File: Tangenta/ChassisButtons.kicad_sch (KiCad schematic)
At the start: 26 parts, among them J2 Conn_02x02_Top_Bottom, Q1 2N7002, Q2 2N7002, SW1 TSC015A04818B, SW2 TSC015A04818B, U7 74HC04D,653, U8 CD4060SA_TR, U9 74HC74D,653

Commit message: Removing component association with previous project (local) libraries.
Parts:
- C34, C35, C36, C37, C38, C39: symbol CholaSymbolsPrjLib:C_Small -> C_Small:C_Small
- J2: symbol CholaSymbolsPrjLib:Conn_02x02_Top_Bottom -> Conn_02x02_Top_Bottom:Conn_02x02_Top_Bottom
- Q1, Q2: footprint CholaFootprintsPrjLib:NMOS_2N7002 -> NMOS_2N7002:NMOS_2N7002; symbol CholaSymbolsPrjLib:2N7002 -> 2N7002:2N7002
- R15, R16, R17, R18, R19, R20, R21, R22, R23, R24, R25, R26: symbol CholaSymbolsPrjLib:R_Small_US -> R_Small_US:R_Small_US
- SW1, SW2: footprint CholaFootprintsPrjLib:Tactile_BTN -> Tactile_BTN:Tactile_BTN; symbol CholaSymbolsPrjLib:TSC015A04818B -> TSC015A04818B:TSC015A04818B
- U7: footprint CholaFootprintsPrjLib:74HC04D -> 74HC04D:74HC04D; symbol CholaSymbolsPrjLib:74HC04D,653 -> 74HC04D,653:74HC04D,653
- U8: footprint CholaFootprintsPrjLib:CD4060 -> CD4060:CD4060; symbol CholaSymbolsPrjLib:CD4060SA_TR -> CD4060SA_TR:CD4060SA_TR
- U9: footprint CholaFootprintsPrjLib:74HC74D -> 74HC74D:74HC74D; symbol CholaSymbolsPrjLib:74HC74D,653 -> 74HC74D,653:74HC74D,653
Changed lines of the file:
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@@
 	)
 	(symbol
-		(lib_id "CholaSymbolsPrjLib:R_Small_US")
+		(lib_id "R_Small_US:R_Small_US")
 		(at 68.58 74.93 0)
 		(unit 1)
@@
 	)
 	(symbol
-		(lib_id "CholaSymbolsPrjLib:74HC04D,653")
+		(lib_id "74HC04D,653:74HC04D,653")
 		(at 141.605 66.04 0)
 		(unit 1)
@@
 			)
 		)
-		(property "Footprint" "CholaFootprintsPrjLib:74HC04D"
+		(property "Footprint" "74HC04D:74HC04D"
 			(at 142.748 82.931 0)
 			(effects
@@
 	)
 	(symbol
-		(lib_id "CholaSymbolsPrjLib:R_Small_US")
+		(lib_id "R_Small_US:R_Small_US")
 		(at 215.265 121.285 90)
 		(unit 1)
@@
 	)
 	(symbol
-		(lib_id "CholaSymbolsPrjLib:C_Small")
+		(lib_id "C_Small:C_Small")
 		(at 142.24 82.55 90)
 		(unit 1)
@@
 	)
 	(symbol
-		(lib_id "CholaSymbolsPrjLib:R_Small_US")
+		(lib_id "R_Small_US:R_Small_US")
 		(at 168.275 116.205 90)
 		(unit 1)
@@
 	)
 	(symbol
-		(lib_id "CholaSymbolsPrjLib:TSC015A04818B")
+		(lib_id "TSC015A04818B:TSC015A04818B")
 		(at 60.833 111.125 90)
 		(unit 1)
@@
 			)
 		)
-		(property "Footprint" "CholaFootprintsPrjLib:Tactile_BTN"
+		(property "Footprint" "Tactile_BTN:Tactile_BTN"
 			(at 71.501 114.554 0)
 			(effects
@@
 	)
 	(symbol
-		(lib_id "CholaSymbolsPrjLib:C_Small")
+		(lib_id "C_Small:C_Small")
 		(at 215.265 82.55 90)
 		(unit 1)
@@
 	)
 	(symbol
-		(lib_id "CholaSymbolsPrjLib:74HC74D,653")
+		(lib_id "74HC74D,653:74HC74D,653")
 		(at 215.011 66.167 0)
 		(unit 1)
@@
 			)
 		)
-		(property "Footprint" "CholaFootprintsPrjLib:74HC74D"
+		(property "Footprint" "74HC74D:74HC74D"
 			(at 216.408 82.931 0)
 			(effects
@@
 	)
 	(symbol
-		(lib_id "CholaSymbolsPrjLib:R_Small_US")
+		(lib_id "R_Small_US:R_Small_US")
 		(at 103.505 83.82 90)
 		(unit 1)
@@
 	)
 	(symbol
-		(lib_id "CholaSymbolsPrjLib:Conn_02x02_Top_Bottom")
+		(lib_id "Conn_02x02_Top_Bottom:Conn_02x02_Top_Bottom")
 		(at 76.2 83.82 0)
 		(unit 1)
@@
 	)
 	(symbol
-		(lib_id "CholaSymbolsPrjLib:CD4060SA_TR")
+		(lib_id "CD4060SA_TR:CD4060SA_TR")
 		(at 141.605 109.855 0)
 		(unit 1)
@@
 			)
 		)
-		(property "Footprint" "CholaFootprintsPrjLib:CD4060"
+		(property "Footprint" "CD4060:CD4060"
 			(at 141.605 128.524 0)
 			(effects
@@
 	)
 	(symbol
-		(lib_id "CholaSymbolsPrjLib:R_Small_US")
+		(lib_id "R_Small_US:R_Small_US")
 		(at 237.49 109.855 0)
 		(unit 1)
@@
 	)
 	(symbol
-		(lib_id "CholaSymbolsPrjLib:R_Small_US")
+		(lib_id "R_Small_US:R_Small_US")
 		(at 86.36 74.93 0)
 		(unit 1)
@@
 	)
 	(symbol
-		(lib_id "CholaSymbolsPrjLib:C_Small")
+		(lib_id "C_Small:C_Small")
 		(at 69.215 111.125 0)
 		(mirror x)
@@
 	)
 	(symbol
-		(lib_id "CholaSymbolsPrjLib:2N7002")
+		(lib_id "2N7002:2N7002")
 		(at 224.155 121.285 0)
 		(unit 1)
@@
 			)
 		)
-		(property "Footprint" "CholaFootprintsPrjLib:NMOS_2N7002"
+		(property "Footprint" "NMOS_2N7002:NMOS_2N7002"
 			(at 215.392 139.954 0)
 			(effects
@@
 	)
 	(symbol
-		(lib_id "CholaSymbolsPrjLib:R_Small_US")
+		(lib_id "R_Small_US:R_Small_US")
 		(at 211.455 128.905 0)
 		(unit 1)
@@
 	)
 	(symbol
-		(lib_id "CholaSymbolsPrjLib:R_Small_US")
+		(lib_id "R_Small_US:R_Small_US")
 		(at 252.73 81.28 0)
 		(unit 1)
@@
 	)
 	(symbol
-		(lib_id "CholaSymbolsPrjLib:R_Small_US")
+		(lib_id "R_Small_US:R_Small_US")
 		(at 191.135 60.96 270)
 		(unit 1)
@@
 	)
 	(symbol
-		(lib_id "CholaSymbolsPrjLib:R_Small_US")
+		(lib_id "R_Small_US:R_Small_US")
 		(at 168.275 111.76 90)
 		(unit 1)
@@
 	)
 	(symbol
-		(lib_id "CholaSymbolsPrjLib:R_Small_US")
+		(lib_id "R_Small_US:R_Small_US")
 		(at 52.07 83.82 90)
 		(unit 1)
@@
 	)
 	(symbol
-		(lib_id "CholaSymbolsPrjLib:R_Small_US")
+		(lib_id "R_Small_US:R_Small_US")
 		(at 241.3 102.235 90)
 		(unit 1)
@@
 	)
 	(symbol
-		(lib_id "CholaSymbolsPrjLib:TSC015A04818B")
+		(lib_id "TSC015A04818B:TSC015A04818B")
 		(at 87.122 111.125 270)
 		(mirror x)
@@
 			)
 		)
-		(property "Footprint" "CholaFootprintsPrjLib:Tactile_BTN"
+		(property "Footprint" "Tactile_BTN:Tactile_BTN"
 			(at 76.454 114.554 0)
 			(effects
@@
 	)
 	(symbol
-		(lib_id "CholaSymbolsPrjLib:C_Small")
+		(lib_id "C_Small:C_Small")
 		(at 168.275 120.65 90)
 		(unit 1)
@@
 	)
 	(symbol
-		(lib_id "CholaSymbolsPrjLib:C_Small")
+		(lib_id "C_Small:C_Small")
 		(at 78.74 111.125 0)
 		(mirror x)
@@
 	)
 	(symbol
-		(lib_id "CholaSymbolsPrjLib:2N7002")
+		(lib_id "2N7002:2N7002")
 		(at 250.19 102.235 0)
 		(unit 1)
@@
 			)
 		)
-		(property "Footprint" "CholaFootprintsPrjLib:NMOS_2N7002"
+		(property "Footprint" "NMOS_2N7002:NMOS_2N7002"
 			(at 241.427 120.904 0)
 			(effects
@@
 	)
 	(symbol
-		(lib_id "CholaSymbolsPrjLib:C_Small")
+		(lib_id "C_Small:C_Small")
 		(at 142.24 127.635 90)
 		(unit 1)

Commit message: Fixes, before checks.
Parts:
- C34, C35, C36, C37, C38, C39: symbol C_Small:C_Small -> Device:C_Small
- J2: symbol Conn_02x02_Top_Bottom:Conn_02x02_Top_Bottom -> Connector_Generic:Conn_02x02_Top_Bottom
- Q1, Q2: symbol 2N7002:2N7002 -> NMOS_2N7002:2N7002
- R15, R16, R17, R18, R19, R20, R21, R22, R23, R24, R25, R26: symbol R_Small_US:R_Small_US -> Device:R_Small_US
- SW1, SW2: symbol TSC015A04818B:TSC015A04818B -> Tactile_BTN:TSC015A04818B
- U7: symbol 74HC04D,653:74HC04D,653 -> 74HC04D:74HC04D,653
- U8: symbol CD4060SA_TR:CD4060SA_TR -> CD4060:CD4060SA_TR
- U9: symbol 74HC74D,653:74HC74D,653 -> 74HC74D:74HC74D,653
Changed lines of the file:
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@@
 	)
 	(symbol
-		(lib_id "R_Small_US:R_Small_US")
+		(lib_id "Device:R_Small_US")
 		(at 68.58 74.93 0)
 		(unit 1)
@@
 	)
 	(symbol
-		(lib_id "74HC04D,653:74HC04D,653")
+		(lib_id "74HC04D:74HC04D,653")
 		(at 141.605 66.04 0)
 		(unit 1)
@@
 	)
 	(symbol
-		(lib_id "R_Small_US:R_Small_US")
+		(lib_id "Device:R_Small_US")
 		(at 215.265 121.285 90)
 		(unit 1)
@@
 	)
 	(symbol
-		(lib_id "C_Small:C_Small")
+		(lib_id "Device:C_Small")
 		(at 142.24 82.55 90)
 		(unit 1)
@@
 	)
 	(symbol
-		(lib_id "R_Small_US:R_Small_US")
+		(lib_id "Device:R_Small_US")
 		(at 168.275 116.205 90)
 		(unit 1)
@@
 	)
 	(symbol
-		(lib_id "TSC015A04818B:TSC015A04818B")
+		(lib_id "Tactile_BTN:TSC015A04818B")
 		(at 60.833 111.125 90)
 		(unit 1)
@@
 	)
 	(symbol
-		(lib_id "C_Small:C_Small")
+		(lib_id "Device:C_Small")
 		(at 215.265 82.55 90)
 		(unit 1)
@@
 	)
 	(symbol
-		(lib_id "74HC74D,653:74HC74D,653")
+		(lib_id "74HC74D:74HC74D,653")
 		(at 215.011 66.167 0)
 		(unit 1)
@@
 	)
 	(symbol
-		(lib_id "R_Small_US:R_Small_US")
+		(lib_id "Device:R_Small_US")
 		(at 103.505 83.82 90)
 		(unit 1)
@@
 	)
 	(symbol
-		(lib_id "Conn_02x02_Top_Bottom:Conn_02x02_Top_Bottom")
+		(lib_id "Connector_Generic:Conn_02x02_Top_Bottom")
 		(at 76.2 83.82 0)
 		(unit 1)
@@
 	)
 	(symbol
-		(lib_id "CD4060SA_TR:CD4060SA_TR")
+		(lib_id "CD4060:CD4060SA_TR")
 		(at 141.605 109.855 0)
 		(unit 1)
@@
 	)
 	(symbol
-		(lib_id "R_Small_US:R_Small_US")
+		(lib_id "Device:R_Small_US")
 		(at 237.49 109.855 0)
 		(unit 1)
@@
 	)
 	(symbol
-		(lib_id "R_Small_US:R_Small_US")
+		(lib_id "Device:R_Small_US")
 		(at 86.36 74.93 0)
 		(unit 1)
@@
 	)
 	(symbol
-		(lib_id "C_Small:C_Small")
+		(lib_id "Device:C_Small")
 		(at 69.215 111.125 0)
 		(mirror x)
@@
 	)
 	(symbol
-		(lib_id "2N7002:2N7002")
+		(lib_id "NMOS_2N7002:2N7002")
 		(at 224.155 121.285 0)
 		(unit 1)
@@
 	)
 	(symbol
-		(lib_id "R_Small_US:R_Small_US")
+		(lib_id "Device:R_Small_US")
 		(at 211.455 128.905 0)
 		(unit 1)
@@
 	)
 	(symbol
-		(lib_id "R_Small_US:R_Small_US")
+		(lib_id "Device:R_Small_US")
 		(at 252.73 81.28 0)
 		(unit 1)
@@
 	)
 	(symbol
-		(lib_id "R_Small_US:R_Small_US")
+		(lib_id "Device:R_Small_US")
 		(at 191.135 60.96 270)
 		(unit 1)
@@
 	)
 	(symbol
-		(lib_id "R_Small_US:R_Small_US")
+		(lib_id "Device:R_Small_US")
 		(at 168.275 111.76 90)
 		(unit 1)
@@
 	)
 	(symbol
-		(lib_id "R_Small_US:R_Small_US")
+		(lib_id "Device:R_Small_US")
 		(at 52.07 83.82 90)
 		(unit 1)
@@
 	)
 	(symbol
-		(lib_id "R_Small_US:R_Small_US")
+		(lib_id "Device:R_Small_US")
 		(at 241.3 102.235 90)
 		(unit 1)
@@
 	)
 	(symbol
-		(lib_id "TSC015A04818B:TSC015A04818B")
+		(lib_id "Tactile_BTN:TSC015A04818B")
 		(at 87.122 111.125 270)
 		(mirror x)
@@
 	)
 	(symbol
-		(lib_id "C_Small:C_Small")
+		(lib_id "Device:C_Small")
 		(at 168.275 120.65 90)
 		(unit 1)
@@
 	)
 	(symbol
-		(lib_id "C_Small:C_Small")
+		(lib_id "Device:C_Small")
 		(at 78.74 111.125 0)
 		(mirror x)
@@
 	)
 	(symbol
-		(lib_id "2N7002:2N7002")
+		(lib_id "NMOS_2N7002:2N7002")
 		(at 250.19 102.235 0)
 		(unit 1)
@@
 	)
 	(symbol
-		(lib_id "C_Small:C_Small")
+		(lib_id "Device:C_Small")
 		(at 142.24 127.635 90)
 		(unit 1)

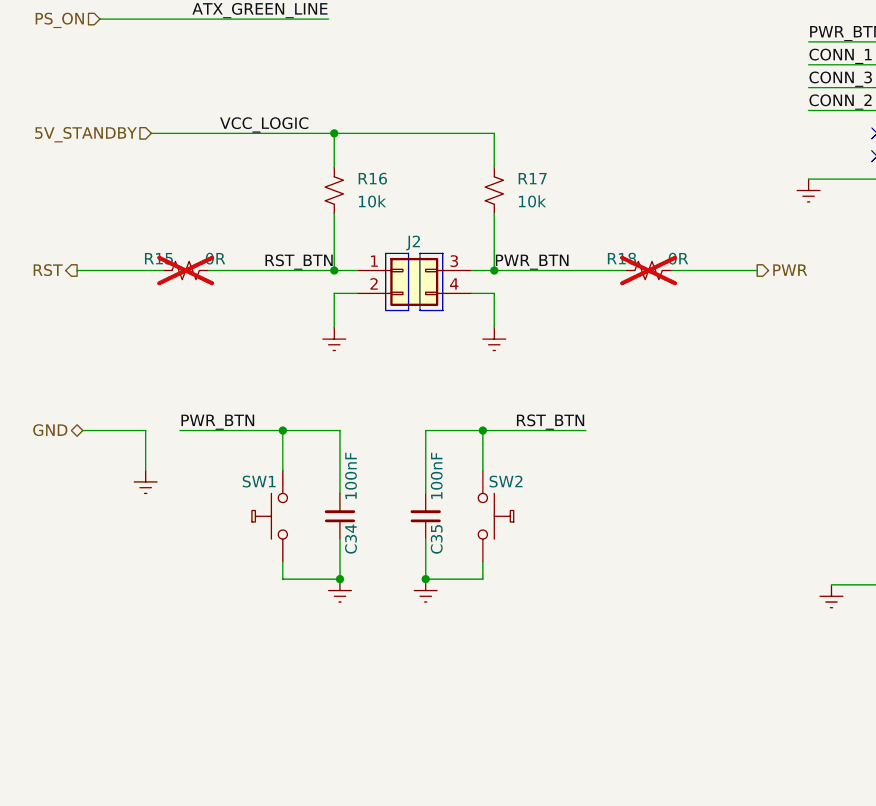
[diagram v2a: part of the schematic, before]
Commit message: Reverting to the original design.
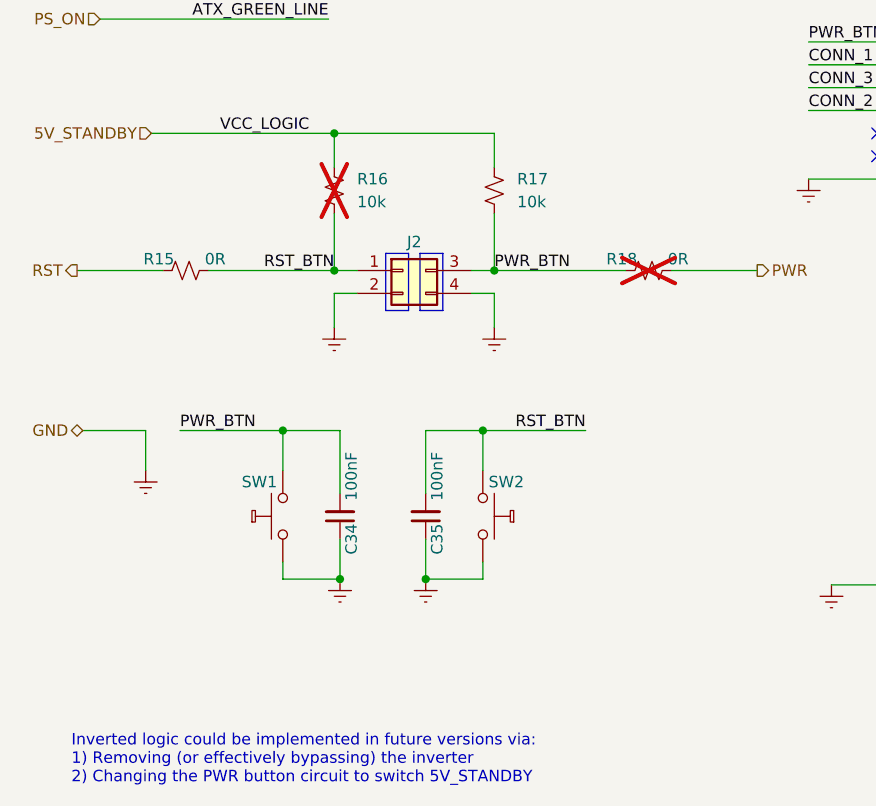
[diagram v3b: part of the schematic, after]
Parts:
- C34, C35, C36, C37, C38, C39: symbol Device:C_Small -> CholaSymbolsPrjLib:C_Small
- J2: symbol Connector_Generic:Conn_02x02_Top_Bottom -> CholaSymbolsPrjLib:Conn_02x02_Top_Bottom
- Q1, Q2: symbol NMOS_2N7002:2N7002 -> CholaSymbolsPrjLib:2N7002
- R15: symbol Device:R_Small_US -> CholaSymbolsPrjLib:R_Small_US; now fitted; now in the parts list
- R16: symbol Device:R_Small_US -> CholaSymbolsPrjLib:R_Small_US; now not fitted; now left out of the parts list
- R17, R18, R19, R20, R21, R22, R23, R24, R25, R26: symbol Device:R_Small_US -> CholaSymbolsPrjLib:R_Small_US
- SW1, SW2: symbol Tactile_BTN:TSC015A04818B -> CholaSymbolsPrjLib:TSC015A04818B
- U7: symbol 74HC04D:74HC04D,653 -> CholaSymbolsPrjLib:74HC04D,653
- U8: symbol CD4060:CD4060SA_TR -> CholaSymbolsPrjLib:CD4060SA_TR
- U9: symbol 74HC74D:74HC74D,653 -> CholaSymbolsPrjLib:74HC74D,653
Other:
- note added: "Inverted logic could be implemented in future versions via: 1) Removing (or effectively bypassing) the inverter 2) Changing the PWR button circuit to switch 5V_STANDBY"

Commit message: ...
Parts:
- C34, C35, C36, C37, C38, C39: symbol CholaSymbolsPrjLib:C_Small -> LocalPrjLib:C_Small
- J2: symbol CholaSymbolsPrjLib:Conn_02x02_Top_Bottom -> LocalPrjLib:Conn_02x02_Top_Bottom
- Q1, Q2: symbol CholaSymbolsPrjLib:2N7002 -> LocalPrjLib:2N7002
- R15, R16, R17, R18, R19, R20, R21, R22, R23, R24, R25, R26: symbol CholaSymbolsPrjLib:R_Small_US -> LocalPrjLib:R_Small_US
- SW1, SW2: symbol CholaSymbolsPrjLib:TSC015A04818B -> LocalPrjLib:TSC015A04818B
- U7: symbol CholaSymbolsPrjLib:74HC04D,653 -> LocalPrjLib:74HC04D,653
- U8: symbol CholaSymbolsPrjLib:CD4060SA_TR -> LocalPrjLib:CD4060SA_TR
- U9: symbol CholaSymbolsPrjLib:74HC74D,653 -> LocalPrjLib:74HC74D,653
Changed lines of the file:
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@@
     )
   )
-  (symbol (lib_id "CholaSymbolsPrjLib:R_Small_US") (at 68.58 74.93 0) (unit 1)
+  (symbol (lib_id "LocalPrjLib:R_Small_US") (at 68.58 74.93 0) (unit 1)
     (in_bom no) (on_board yes) (dnp yes) (fields_autoplaced)
     (property "Reference" "R16" (at 71.12 73.66 0)
@@
     )
   )
-  (symbol (lib_id "CholaSymbolsPrjLib:74HC04D,653") (at 141.605 66.04 0) (unit 1)
+  (symbol (lib_id "LocalPrjLib:74HC04D,653") (at 141.605 66.04 0) (unit 1)
     (in_bom yes) (on_board yes) (dnp no)
     (property "Reference" "U7" (at 135.255 54.61 0)
@@
     )
   )
-  (symbol (lib_id "CholaSymbolsPrjLib:R_Small_US") (at 215.265 121.285 90) (unit 1)
+  (symbol (lib_id "LocalPrjLib:R_Small_US") (at 215.265 121.285 90) (unit 1)
     (in_bom yes) (on_board yes) (dnp no)
     (property "Reference" "R23" (at 212.725 120.015 90)
@@
     )
   )
-  (symbol (lib_id "CholaSymbolsPrjLib:C_Small") (at 142.24 82.55 90) (unit 1)
+  (symbol (lib_id "LocalPrjLib:C_Small") (at 142.24 82.55 90) (unit 1)
     (in_bom yes) (on_board yes) (dnp no)
     (property "Reference" "C36" (at 139.065 83.82 90)
@@
     )
   )
-  (symbol (lib_id "CholaSymbolsPrjLib:R_Small_US") (at 168.275 116.205 90) (unit 1)
+  (symbol (lib_id "LocalPrjLib:R_Small_US") (at 168.275 116.205 90) (unit 1)
     (in_bom yes) (on_board yes) (dnp no)
     (property "Reference" "R20" (at 165.735 114.935 90)
@@
     )
   )
-  (symbol (lib_id "CholaSymbolsPrjLib:TSC015A04818B") (at 60.833 111.125 90) (unit 1)
+  (symbol (lib_id "LocalPrjLib:TSC015A04818B") (at 60.833 111.125 90) (unit 1)
     (in_bom yes) (on_board yes) (dnp no)
     (property "Reference" "SW1" (at 58.293 107.315 90)
@@
     )
   )
-  (symbol (lib_id "CholaSymbolsPrjLib:C_Small") (at 215.265 82.55 90) (unit 1)
+  (symbol (lib_id "LocalPrjLib:C_Small") (at 215.265 82.55 90) (unit 1)
     (in_bom yes) (on_board yes) (dnp no)
     (property "Reference" "C39" (at 212.09 83.82 90)
@@
     )
   )
-  (symbol (lib_id "CholaSymbolsPrjLib:74HC74D,653") (at 215.011 66.167 0) (unit 1)
+  (symbol (lib_id "LocalPrjLib:74HC74D,653") (at 215.011 66.167 0) (unit 1)
     (in_bom yes) (on_board yes) (dnp no)
     (property "Reference" "U9" (at 208.661 54.737 0)
@@
     )
   )
-  (symbol (lib_id "CholaSymbolsPrjLib:R_Small_US") (at 103.505 83.82 90) (unit 1)
+  (symbol (lib_id "LocalPrjLib:R_Small_US") (at 103.505 83.82 90) (unit 1)
     (in_bom no) (on_board yes) (dnp yes)
     (property "Reference" "R18" (at 102.235 82.55 90)
@@
     )
   )
-  (symbol (lib_id "CholaSymbolsPrjLib:Conn_02x02_Top_Bottom") (at 76.2 83.82 0) (unit 1)
+  (symbol (lib_id "LocalPrjLib:Conn_02x02_Top_Bottom") (at 76.2 83.82 0) (unit 1)
     (in_bom yes) (on_board yes) (dnp no)
     (property "Reference" "J2" (at 77.47 80.645 0)
@@
     )
   )
-  (symbol (lib_id "CholaSymbolsPrjLib:CD4060SA_TR") (at 141.605 109.855 0) (unit 1)
+  (symbol (lib_id "LocalPrjLib:CD4060SA_TR") (at 141.605 109.855 0) (unit 1)
     (in_bom yes) (on_board yes) (dnp no)
     (property "Reference" "U8" (at 135.255 97.155 0)
@@
     )
   )
-  (symbol (lib_id "CholaSymbolsPrjLib:R_Small_US") (at 237.49 109.855 0) (unit 1)
+  (symbol (lib_id "LocalPrjLib:R_Small_US") (at 237.49 109.855 0) (unit 1)
     (in_bom yes) (on_board yes) (dnp no)
     (property "Reference" "R24" (at 238.76 108.585 0)
@@
     )
   )
-  (symbol (lib_id "CholaSymbolsPrjLib:R_Small_US") (at 86.36 74.93 0) (unit 1)
+  (symbol (lib_id "LocalPrjLib:R_Small_US") (at 86.36 74.93 0) (unit 1)
     (in_bom yes) (on_board yes) (dnp no) (fields_autoplaced)
     (property "Reference" "R17" (at 88.9 73.66 0)
@@
     )
   )
-  (symbol (lib_id "CholaSymbolsPrjLib:C_Small") (at 69.215 111.125 0) (mirror x) (unit 1)
+  (symbol (lib_id "LocalPrjLib:C_Small") (at 69.215 111.125 0) (mirror x) (unit 1)
     (in_bom yes) (on_board yes) (dnp no)
     (property "Reference" "C34" (at 70.485 113.665 90)
@@
     )
   )
-  (symbol (lib_id "CholaSymbolsPrjLib:2N7002") (at 224.155 121.285 0) (unit 1)
+  (symbol (lib_id "LocalPrjLib:2N7002") (at 224.155 121.285 0) (unit 1)
     (in_bom yes) (on_board yes) (dnp no)
     (property "Reference" "Q1" (at 227.33 117.475 0)
@@
     )
   )
-  (symbol (lib_id "CholaSymbolsPrjLib:R_Small_US") (at 211.455 128.905 0) (unit 1)
+  (symbol (lib_id "LocalPrjLib:R_Small_US") (at 211.455 128.905 0) (unit 1)
     (in_bom yes) (on_board yes) (dnp no)
     (property "Reference" "R22" (at 212.725 127.635 0)
@@
     )
   )
-  (symbol (lib_id "CholaSymbolsPrjLib:R_Small_US") (at 252.73 81.28 0) (unit 1)
+  (symbol (lib_id "LocalPrjLib:R_Small_US") (at 252.73 81.28 0) (unit 1)
     (in_bom yes) (on_board yes) (dnp no)
     (property "Reference" "R26" (at 254 77.47 90)
@@
     )
   )
-  (symbol (lib_id "CholaSymbolsPrjLib:R_Small_US") (at 191.135 60.96 270) (unit 1)
+  (symbol (lib_id "LocalPrjLib:R_Small_US") (at 191.135 60.96 270) (unit 1)
     (in_bom yes) (on_board yes) (dnp no)
     (property "Reference" "R21" (at 188.595 59.69 90)
@@
     )
   )
-  (symbol (lib_id "CholaSymbolsPrjLib:R_Small_US") (at 168.275 111.76 90) (unit 1)
+  (symbol (lib_id "LocalPrjLib:R_Small_US") (at 168.275 111.76 90) (unit 1)
     (in_bom yes) (on_board yes) (dnp no)
     (property "Reference" "R19" (at 165.735 110.49 90)
@@
     )
   )
-  (symbol (lib_id "CholaSymbolsPrjLib:R_Small_US") (at 52.07 83.82 90) (unit 1)
+  (symbol (lib_id "LocalPrjLib:R_Small_US") (at 52.07 83.82 90) (unit 1)
     (in_bom yes) (on_board yes) (dnp no)
     (property "Reference" "R15" (at 50.8 82.55 90)
@@
     )
   )
-  (symbol (lib_id "CholaSymbolsPrjLib:R_Small_US") (at 241.3 102.235 90) (unit 1)
+  (symbol (lib_id "LocalPrjLib:R_Small_US") (at 241.3 102.235 90) (unit 1)
     (in_bom yes) (on_board yes) (dnp no)
     (property "Reference" "R25" (at 238.76 100.965 90)
@@
     )
   )
-  (symbol (lib_id "CholaSymbolsPrjLib:TSC015A04818B") (at 87.122 111.125 270) (mirror x) (unit 1)
+  (symbol (lib_id "LocalPrjLib:TSC015A04818B") (at 87.122 111.125 270) (mirror x) (unit 1)
     (in_bom yes) (on_board yes) (dnp no)
     (property "Reference" "SW2" (at 89.662 107.315 90)
@@
     )
   )
-  (symbol (lib_id "CholaSymbolsPrjLib:C_Small") (at 168.275 120.65 90) (unit 1)
+  (symbol (lib_id "LocalPrjLib:C_Small") (at 168.275 120.65 90) (unit 1)
     (in_bom yes) (on_board yes) (dnp no)
     (property "Reference" "C38" (at 165.735 119.38 90)
@@
     )
   )
-  (symbol (lib_id "CholaSymbolsPrjLib:C_Small") (at 78.74 111.125 0) (mirror x) (unit 1)
+  (symbol (lib_id "LocalPrjLib:C_Small") (at 78.74 111.125 0) (mirror x) (unit 1)
     (in_bom yes) (on_board yes) (dnp no)
     (property "Reference" "C35" (at 80.01 113.665 90)
@@
     )
   )
-  (symbol (lib_id "CholaSymbolsPrjLib:2N7002") (at 250.19 102.235 0) (unit 1)
+  (symbol (lib_id "LocalPrjLib:2N7002") (at 250.19 102.235 0) (unit 1)
     (in_bom yes) (on_board yes) (dnp no) (fields_autoplaced)
     (property "Reference" "Q2" (at 257.81 100.965 0)
@@
     )
   )
-  (symbol (lib_id "CholaSymbolsPrjLib:C_Small") (at 142.24 127.635 90) (unit 1)
+  (symbol (lib_id "LocalPrjLib:C_Small") (at 142.24 127.635 90) (unit 1)
     (in_bom yes) (on_board yes) (dnp no)
     (property "Reference" "C37" (at 139.065 128.905 90)
